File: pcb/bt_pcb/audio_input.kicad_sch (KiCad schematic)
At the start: 52 parts, among them IC6 ADG736BRM, IC7 ADG736BRM, J5 AudioJack3_Switch, J8 AudioJack3_Switch, U6 MCP6004, U7 MCP6004

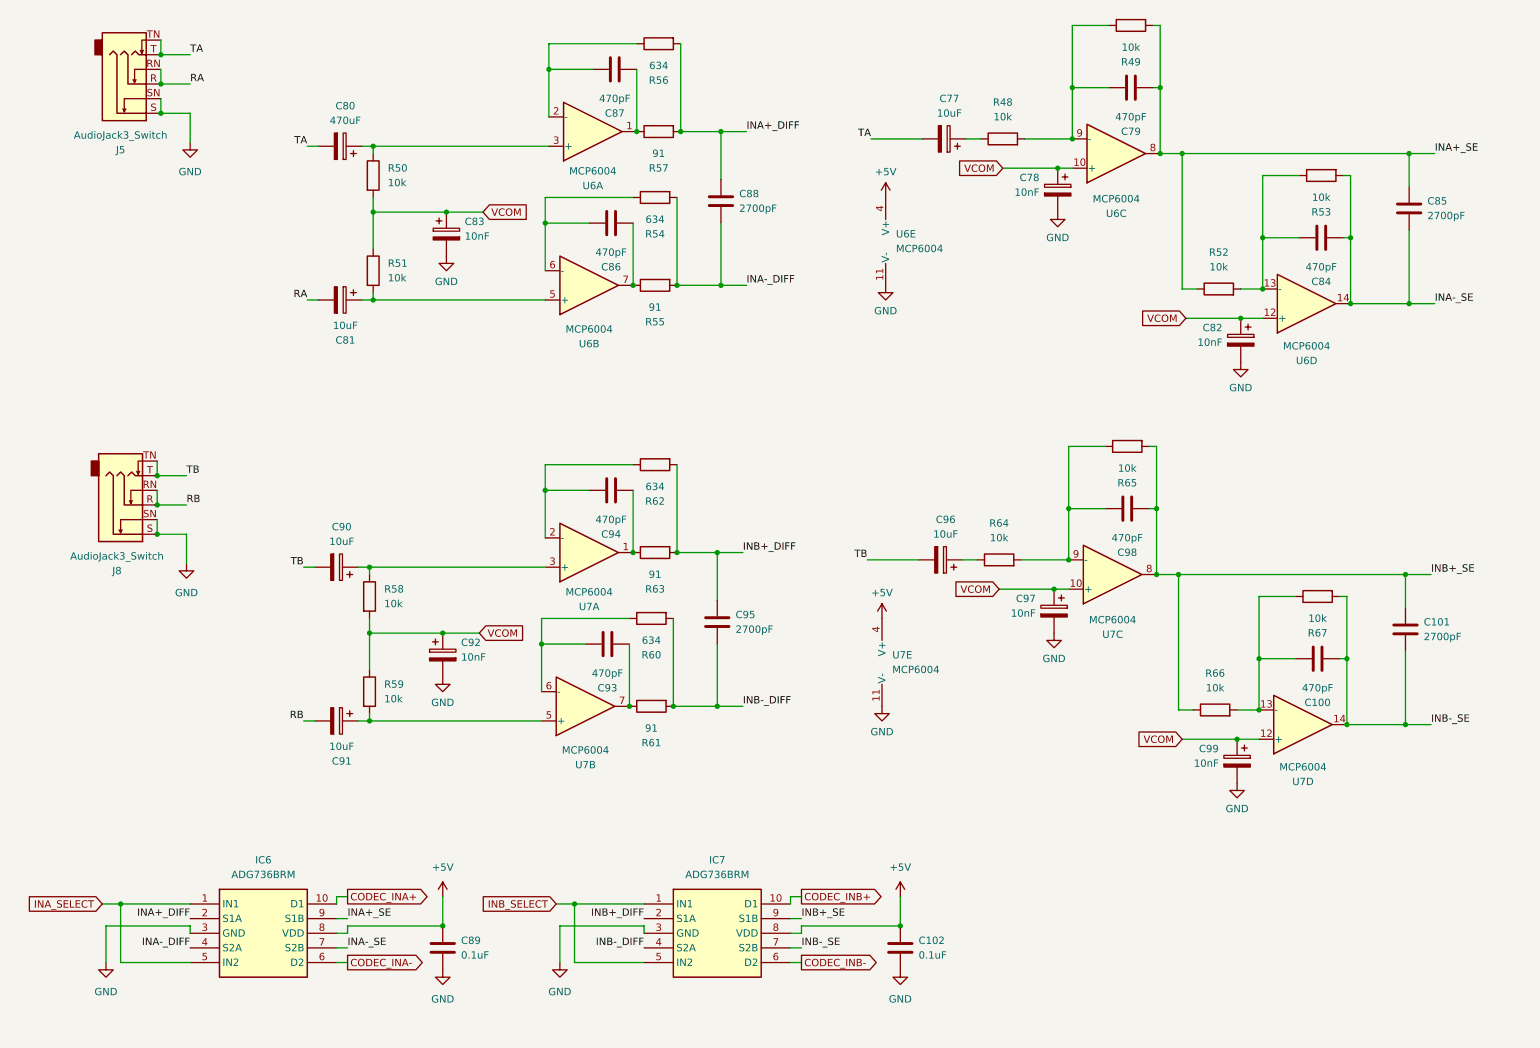
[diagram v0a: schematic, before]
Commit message: ditching power pcb, new codec
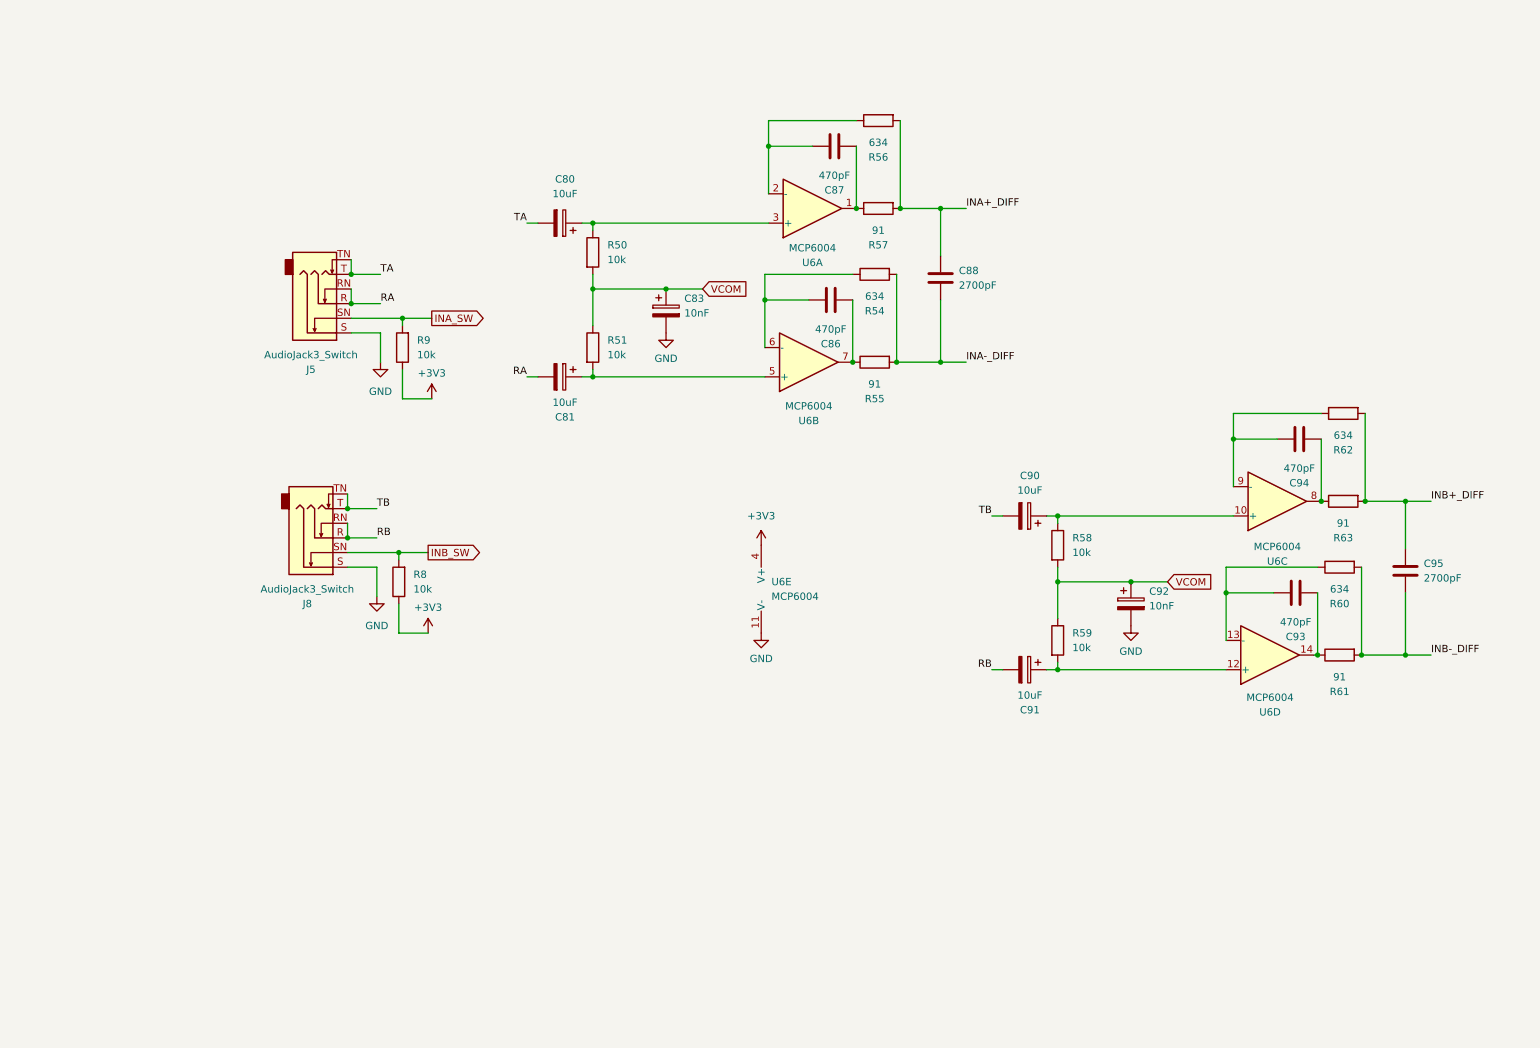
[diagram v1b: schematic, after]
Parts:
- removed C100, C79, C84, C98: 470pF, symbol Device:C
- removed C101, C85: 2700pF, symbol Device:C
- removed C102, C89: 0.1uF, symbol Device:C
- removed C77, C96: 10uF, symbol Device:C_Polarized
- removed C78, C82, C97, C99: 10nF, symbol Device:C_Polarized
- removed IC6, IC7: ADG736BRM, library:SOP50P490X110-10N, symbol library:ADG736BRM
- removed R48, R49, R52, R53, R64, R65, R66, R67: 10k, symbol Device:R
- removed U7: MCP6004, symbol Amplifier_Operational:MCP6004
- added R8, R9: 10k, symbol Device:R
- C80: value 470uF -> 10uF
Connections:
- net INA+_SE is gone; now on an unnamed net: U6.8
- net INA-_SE is gone; now on an unnamed net: U6.14
- net GND: no longer J5.SN, J8.SN
- net VCOM: no longer U6.10 (+), U6.12 (+)
- net at U6.9 (-): now also C94.2, R62.1
- net at C91.1, R59.2: now also U6.12 (+)
- net at C93.2, R60.1: now also U6.13 (-)
- net at C90.1, R58.1: now also U6.10 (+)
- net +5V renamed +3V3
- net +3V3: now also R8.1, R9.1
- new net INA_SW: J5.SN, R9.2
- new net INB_SW: J8.SN, R8.2
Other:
- moved on the sheet: C80, C81, C83, C86, C87, C88, C90, C91, C92, C93, C94, C95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

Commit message: big progress, now revising error and warnings
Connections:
- net +3V3: no longer U6.4 (V+)
- net INA+_DIFF renamed CODEC_INA+
- net INA-_DIFF renamed CODEC_INA-
- net INB+_DIFF renamed CODEC_INB+
- net INB-_DIFF renamed CODEC_INB-
- new net +3V3A: U6.4 (V+)
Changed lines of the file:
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@@
-		)
-	)
-	(label "INA+_DIFF"
-		(at 175.895 48.26 0)
-		(effects
-			(font
-				(size 1.27 1.27)
-			)
-			(justify left bottom)
 		)
 	)
@@
 		)
 	)
-	(label "INB-_DIFF"
-		(at 256.54 125.73 0)
-		(effects
-			(font
-				(size 1.27 1.27)
-			)
-			(justify left bottom)
-		)
-	)
 	(label "TB"
 		(at 73.66 100.33 0)
@@
 	(label "RA"
 		(at 74.295 64.77 0)
-		(effects
-			(font
-				(size 1.27 1.27)
-			)
-			(justify left bottom)
-		)
-	)
-	(label "INA-_DIFF"
-		(at 175.895 74.93 0)
-		(effects
-			(font
-				(size 1.27 1.27)
-			)
-			(justify left bottom)
-		)
-	)
-	(label "INB+_DIFF"
-		(at 256.54 99.06 0)
 		(effects
 			(font
@@
 	)
 	(global_label "INB_SW"
+		(shape passive)
+		(at 82.55 107.95 0)
+		(fields_autoplaced yes)
+		(effects
+			(font
+				(size 1.27 1.27)
+			)
+			(justify left)
+		)
+		(property "Intersheetrefs" "${INTERSHEET_REFS}"
+			(at 91.2577 107.95 0)
+			(effects
+				(font
+					(size 1.27 1.27)
+				)
+				(justify left)
+				(hide yes)
+			)
+		)
+	)
+	(global_label "INA_SW"
+		(shape passive)
+		(at 83.185 67.31 0)
+		(fields_autoplaced yes)
+		(effects
+			(font
+				(size 1.27 1.27)
+			)
+			(justify left)
+		)
+		(property "Intersheetrefs" "${INTERSHEET_REFS}"
+			(at 91.7113 67.31 0)
+			(effects
+				(font
+					(size 1.27 1.27)
+				)
+				(justify left)
+				(hide yes)
+			)
+		)
+	)
+	(global_label "CODEC_INA+"
 		(shape output)
-		(at 82.55 107.95 0)
-		(fields_autoplaced yes)
-		(effects
-			(font
-				(size 1.27 1.27)
-			)
-			(justify left)
-		)
-		(property "Intersheetrefs" "${INTERSHEET_REFS}"
-			(at 92.369 107.95 0)
-			(effects
-				(font
-					(size 1.27 1.27)
-				)
-				(justify left)
-				(hide yes)
-			)
-		)
-	)
-	(global_label "INA_SW"
-		(shape output)
-		(at 83.185 67.31 0)
-		(fields_autoplaced yes)
-		(effects
-			(font
-				(size 1.27 1.27)
-			)
-			(justify left)
-		)
-		(property "Intersheetrefs" "${INTERSHEET_REFS}"
-			(at 92.8226 67.31 0)
+		(at 175.895 48.26 0)
+		(fields_autoplaced yes)
+		(effects
+			(font
+				(size 1.27 1.27)
+			)
+			(justify left)
+		)
+		(property "Intersheetrefs" "${INTERSHEET_REFS}"
+			(at 190.7336 48.26 0)
 			(effects
 				(font
@@
 		(property "Intersheetrefs" "${INTERSHEET_REFS}"
 			(at 138.3007 62.23 0)
+			(effects
+				(font
+					(size 1.27 1.27)
+				)
+				(justify left)
+				(hide yes)
+			)
+		)
+	)
+	(global_label "CODEC_INB-"
+		(shape output)
+		(at 256.54 125.73 0)
+		(fields_autoplaced yes)
+		(effects
+			(font
+				(size 1.27 1.27)
+			)
+			(justify left)
+		)
+		(property "Intersheetrefs" "${INTERSHEET_REFS}"
+			(at 271.56 125.73 0)
+			(effects
+				(font
+					(size 1.27 1.27)
+				)
+				(justify left)
+				(hide yes)
+			)
+		)
+	)
+	(global_label "CODEC_INB+"
+		(shape output)
+		(at 256.54 99.06 0)
+		(fields_autoplaced yes)
+		(effects
+			(font
+				(size 1.27 1.27)
+			)
+			(justify left)
+		)
+		(property "Intersheetrefs" "${INTERSHEET_REFS}"
+			(at 271.56 99.06 0)
+			(effects
+				(font
+					(size 1.27 1.27)
+				)
+				(justify left)
+				(hide yes)
+			)
+		)
+	)
+	(global_label "CODEC_INA-"
+		(shape output)
+		(at 175.895 74.93 0)
+		(fields_autoplaced yes)
+		(effects
+			(font
+				(size 1.27 1.27)
+			)
+			(justify left)
+		)
+		(property "Intersheetrefs" "${INTERSHEET_REFS}"
+			(at 190.7336 74.93 0)
 			(effects
 				(font
@@
 			)
 		)
-		(property "Value" "+3V3"
+		(property "Value" "+3V3A"
 			(at 140.335 101.6 0)
 			(effects

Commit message: solving some erc warnings and errors
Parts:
- renumbered C80 to C74, C81 to C75, C83 to C76, C86 to C77, C87 to C78, C88 to C79, C90 to C80, C91 to C81, C92 to C82, C94 to C83, C93 to C84, C95 to C85, J8 to J17, J5 to J18, R8 to R57, R9 to R58, R50 to R59, R51 to R60, R54 to R61, R55 to R62, R56 to R63, R57 to R64, R58 to R65, R59 to R66, R62 to R67, R63 to R68, R60 to R69, R61 to R70, U6 to U4
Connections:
- net +3V3A renamed +3.3VA
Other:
- moved on the sheet: C76, C77, C78, C79, C80, C81, C83, C84, C85, J18, R58, R59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

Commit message: schematic in theory finished
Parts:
- added R76, R77, R79, R80: 0, Resistor_SMD:R_0603_1608Metric_Pad0.98x0.95mm_HandSolder, symbol Device:R
- C74: renamed from C78; value 470pF -> 470p; footprint (none) -> Capacitor_SMD:C_0603_1608Metric_Pad1.08x0.95mm_HandSolder
- C75: renamed from C74; value 10uF -> 10u; footprint (none) -> Capacitor_SMD:C_0805_2012Metric_Pad1.18x1.45mm_HandSolder
- C76: renamed from C79; value 2700pF -> 2.7n; footprint (none) -> Capacitor_SMD:C_0603_1608Metric_Pad1.08x0.95mm_HandSolder
- C77: value 470pF -> 470p; footprint (none) -> Capacitor_SMD:C_0603_1608Metric_Pad1.08x0.95mm_HandSolder
- C78: renamed from C76; value 10nF -> 10n; footprint (none) -> Capacitor_SMD:C_0603_1608Metric_Pad1.08x0.95mm_HandSolder
- C79: renamed from C75; value 10uF -> 10u; footprint (none) -> Capacitor_SMD:C_0805_2012Metric_Pad1.18x1.45mm_HandSolder
- C80: renamed from C83; value 470pF -> 470p; footprint (none) -> Capacitor_SMD:C_0603_1608Metric_Pad1.08x0.95mm_HandSolder
- C81: renamed from C80; value 10uF -> 10u; footprint (none) -> Capacitor_SMD:C_0805_2012Metric_Pad1.18x1.45mm_HandSolder
- C82: renamed from C85; value 2700pF -> 2.7n; footprint (none) -> Capacitor_SMD:C_0603_1608Metric_Pad1.08x0.95mm_HandSolder
- C83: renamed from C84; value 470pF -> 470p; footprint (none) -> Capacitor_SMD:C_0603_1608Metric_Pad1.08x0.95mm_HandSolder
- C84: renamed from C82; value 10nF -> 10n; footprint (none) -> Capacitor_SMD:C_0603_1608Metric_Pad1.08x0.95mm_HandSolder
- C85: renamed from C81; value 10uF -> 10u; footprint (none) -> Capacitor_SMD:C_0805_2012Metric_Pad1.18x1.45mm_HandSolder
- J15: renamed from J18; value AudioJack3_Switch -> ReanNYS216G; footprint (none) -> library:NYS-216G
- J16: renamed from J17; value AudioJack3_Switch -> ReanNYS216G; footprint (none) -> library:NYS-216G
- R63, R64: footprint (none) -> Resistor_SMD:R_0603_1608Metric_Pad0.98x0.95mm_HandSolder
- R65: renamed from R59; footprint (none) -> Resistor_SMD:R_0603_1608Metric_Pad0.98x0.95mm_HandSolder
- R66: renamed from R61; footprint (none) -> Resistor_SMD:R_0603_1608Metric_Pad0.98x0.95mm_HandSolder
- R67: renamed from R60; footprint (none) -> Resistor_SMD:R_0603_1608Metric_Pad0.98x0.95mm_HandSolder
- R68: renamed from R62; footprint (none) -> Resistor_SMD:R_0603_1608Metric_Pad0.98x0.95mm_HandSolder
- R69: renamed from R67; footprint (none) -> Resistor_SMD:R_0603_1608Metric_Pad0.98x0.95mm_HandSolder
- R70: renamed from R68; footprint (none) -> Resistor_SMD:R_0603_1608Metric_Pad0.98x0.95mm_HandSolder
- R71: renamed from R65; footprint (none) -> Resistor_SMD:R_0603_1608Metric_Pad0.98x0.95mm_HandSolder
- R72: renamed from R69; footprint (none) -> Resistor_SMD:R_0603_1608Metric_Pad0.98x0.95mm_HandSolder
- R73: renamed from R66; footprint (none) -> Resistor_SMD:R_0603_1608Metric_Pad0.98x0.95mm_HandSolder
- R74: renamed from R70; footprint (none) -> Resistor_SMD:R_0603_1608Metric_Pad0.98x0.95mm_HandSolder
- R75: renamed from R58; footprint (none) -> Resistor_SMD:R_0603_1608Metric_Pad0.98x0.95mm_HandSolder
- R78: renamed from R57; footprint (none) -> Resistor_SMD:R_0603_1608Metric_Pad0.98x0.95mm_HandSolder
- U4: footprint (none) -> Package_SO:TSSOP-14_4.4x5mm_P0.65mm
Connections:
- net +3V3: now also R75.2, R78.2; no longer R75.1, R78.1
- net GND: now also J15.RN, J15.TN, J16.RN, J16.TN, R77.2, R80.2
- net INA_SW: now also R76.1; no longer J15.SN, R75.2
- net INB_SW: now also R79.1; no longer J16.SN, R78.2
- net RA: no longer J15.RN
- net RB: no longer J16.RN
- net TA: no longer J15.TN
- net TB: no longer J16.TN
- new net: J16.SN, R78.1, R79.2, R80.1
- new net: J15.SN, R75.1, R76.2, R77.1
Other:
- note added: "In theory: close switch open ground"
- moved on the sheet: C74, C75, C76, C77, C78, C79, C80, C81, C82, C83, C84, C85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

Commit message: pcb started
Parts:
- renumbered J15 to J18, J16 to J19, R63 to R64, R64 to R65, R65 to R66, R66 to R67, R67 to R68, R68 to R69, R69 to R70, R70 to R71, R71 to R72, R72 to R73, R73 to R74, R74 to R75, R75 to R76, R76 to R77, R77 to R78, R78 to R79, R79 to R80, R80 to R81

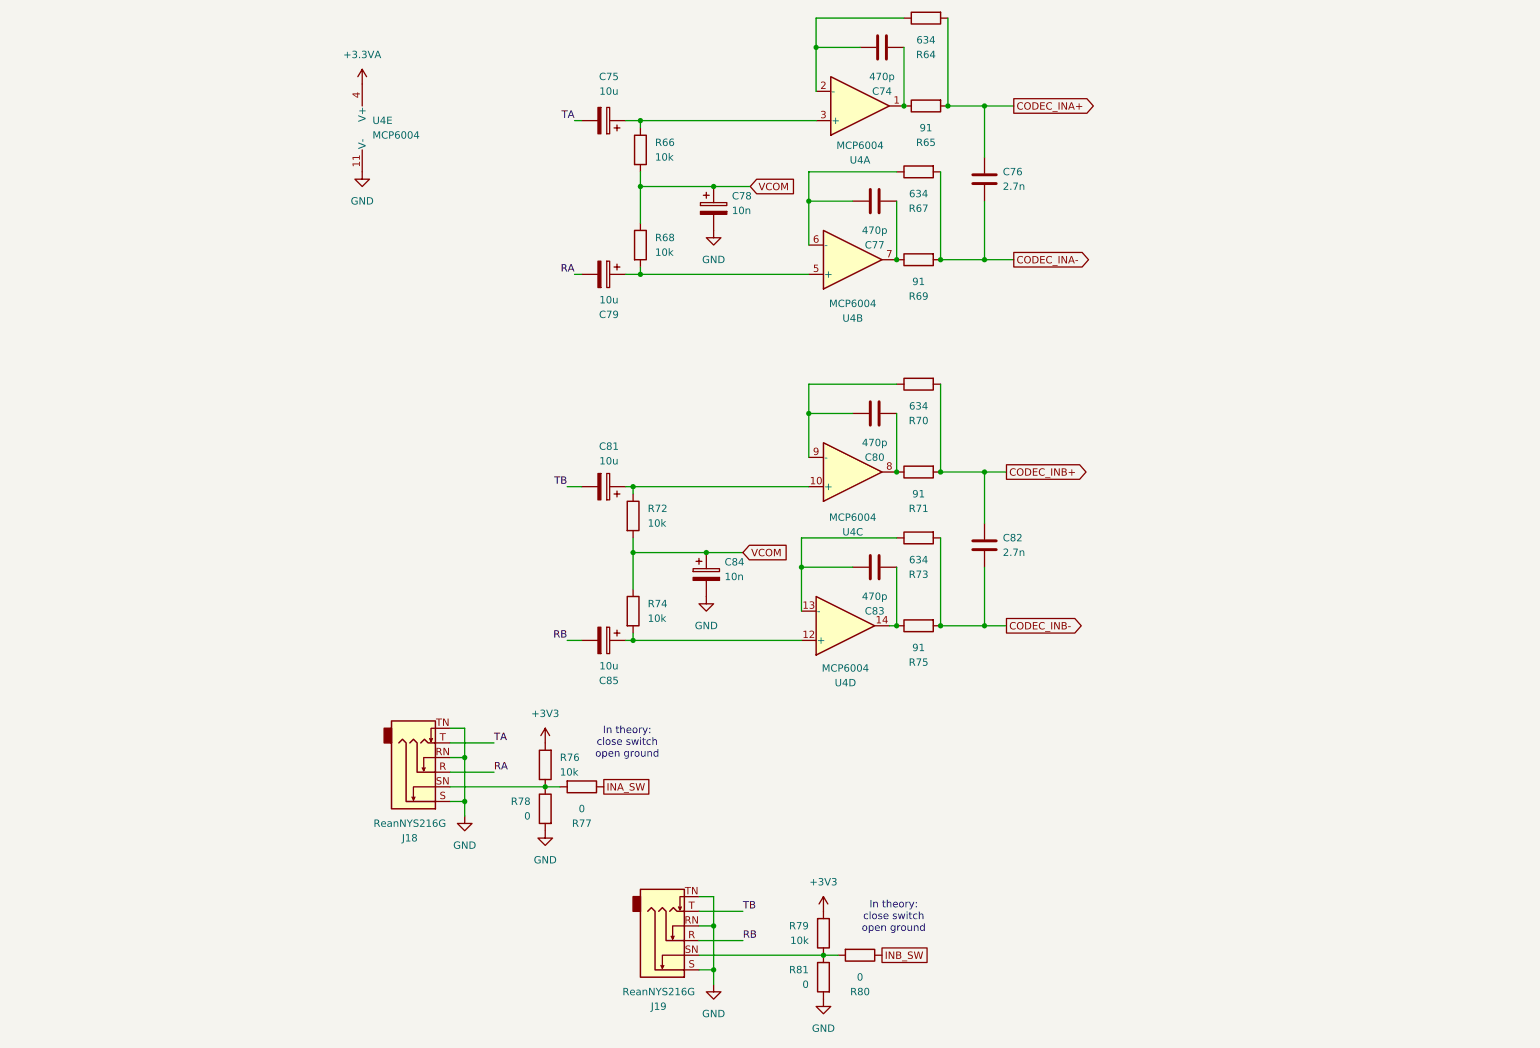
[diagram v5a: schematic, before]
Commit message: pcb with some schematic tuning
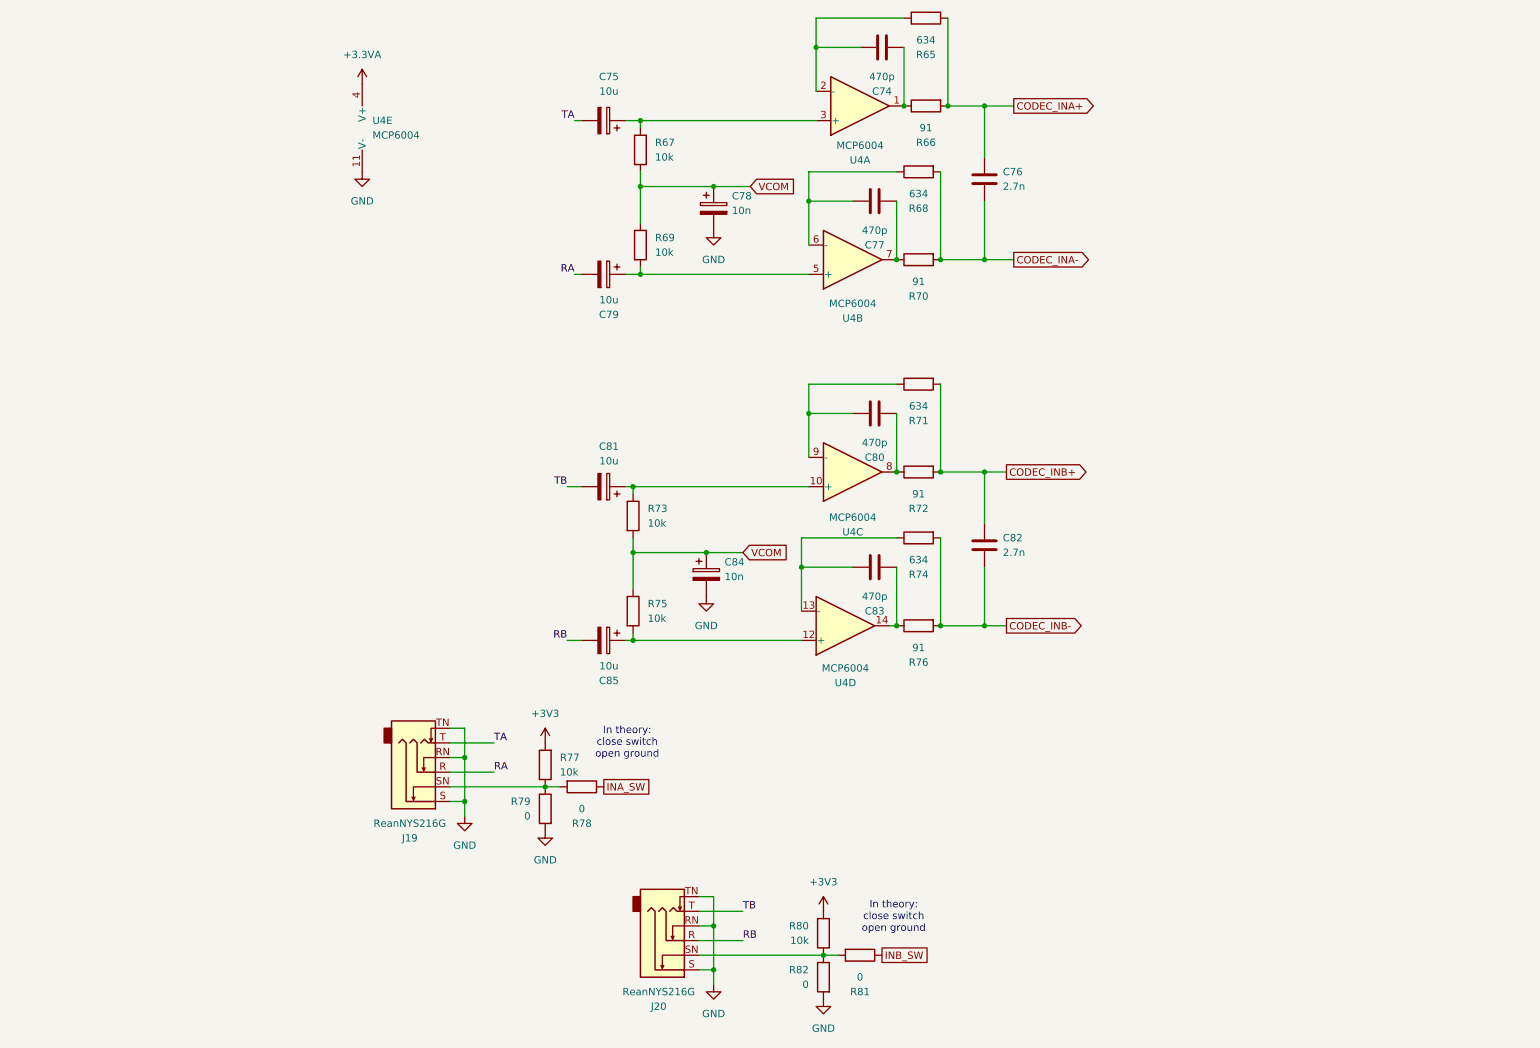
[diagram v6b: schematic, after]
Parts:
- renumbered J18 to J19, J19 to J20, R64 to R65, R65 to R66, R66 to R67, R67 to R68, R68 to R69, R69 to R70, R70 to R71, R71 to R72, R72 to R73, R73 to R74, R74 to R75, R75 to R76, R76 to R77, R77 to R78, R78 to R79, R79 to R80, R80 to R81, R81 to R82

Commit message: pcb now under revision
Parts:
- renumbered C74 to C78, C75 to C79, C76 to C80, C77 to C81, C78 to C82, C79 to C83, C80 to C84, C81 to C85, C82 to C86, C83 to C87, C84 to C88, C85 to C89, R65 to R66, R66 to R67, R67 to R68, R68 to R69, R69 to R70, R70 to R71, R71 to R72, R72 to R73, R73 to R74, R74 to R75, R75 to R76, R76 to R77, R77 to R78, R78 to R79, R79 to R80, R80 to R81, R81 to R82, R82 to R83

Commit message: first notes
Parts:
- renumbered C78 to C68, C79 to C69, C80 to C70, C81 to C71, C82 to C72, C83 to C73, C84 to C74, C85 to C75, C86 to C76, C87 to C77, C88 to C78, C89 to C79, R66 to R67, R67 to R68, R68 to R69, R69 to R70, R70 to R71, R71 to R72, R72 to R73, R73 to R74, R74 to R75, R75 to R76, R76 to R77, R77 to R78, R78 to R79, R79 to R80, R80 to R81, R81 to R82, R82 to R83, R83 to R84
